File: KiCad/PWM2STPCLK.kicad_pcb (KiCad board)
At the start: 2 copper layers, 21.8 x 16 mm, 8 parts, among them J1 PWM, J2 STPCLK, J3 STPCLK, Q1 2N7002

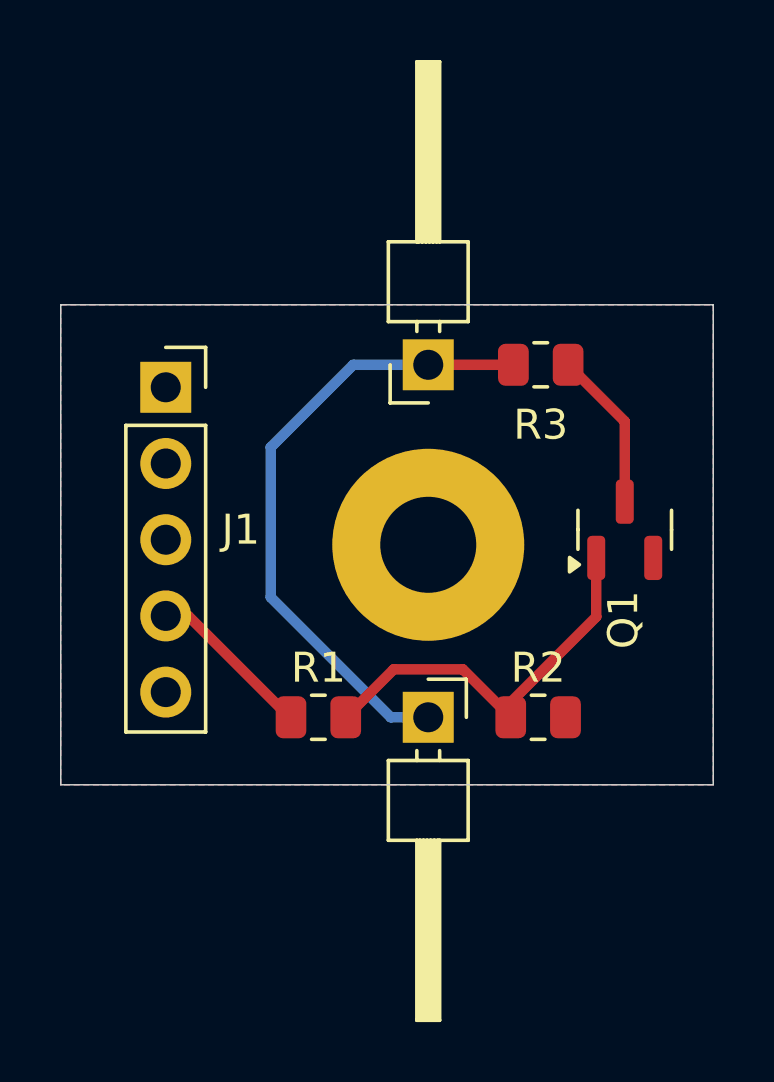
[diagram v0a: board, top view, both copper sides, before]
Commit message: v0.2 - Low resistance ground, cleaner layout
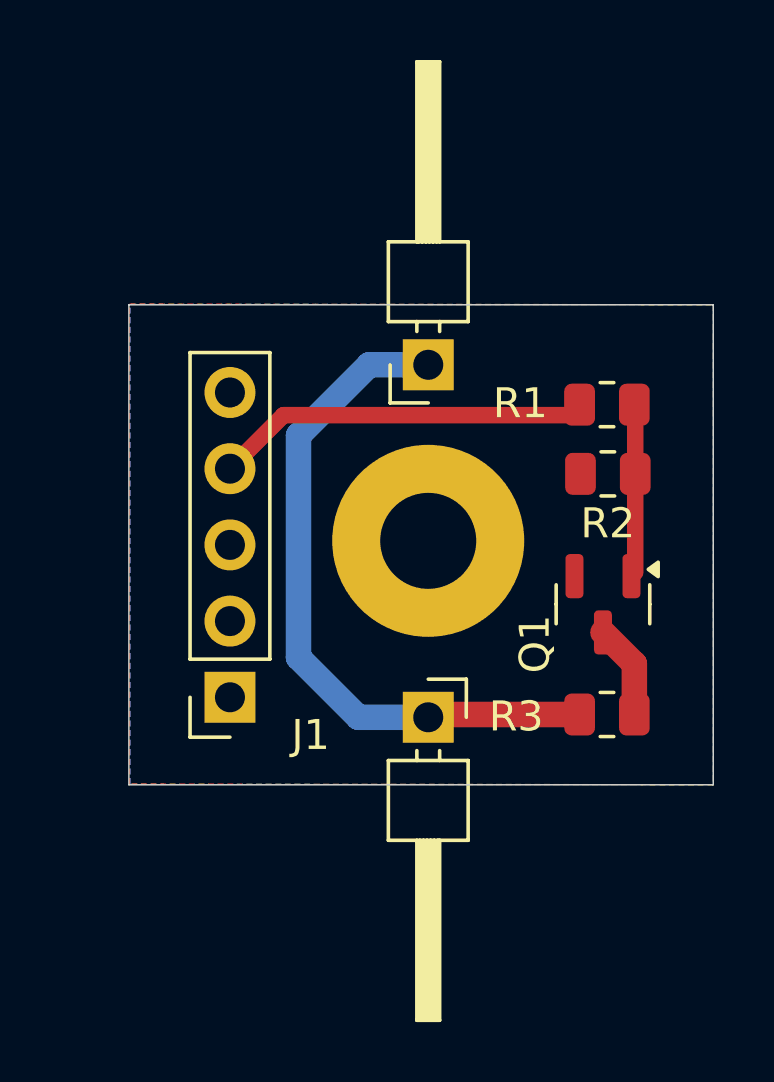
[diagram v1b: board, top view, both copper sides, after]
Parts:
- moved R1 14.2 mm to (157.2, 80.1)
- moved R3 11.9 mm to (157.2, 90.4)
- moved J1 10.6 mm to (144.6, 89.8), turned to 180 degrees
- moved R2 8.44 mm to (157.2, 82.4), turned to 180 degrees
- moved Q1 2.59 mm to (157.1, 86.7), turned to -90 degrees
- moved H1 0.13 mm to (151.2, 84.6)
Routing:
- net Net-(Q1-G): track 13.3 -> 5.78 mm
- net PWM: track 5.58 -> 12.5 mm
- net Net-(Q1-D): track 5.34 -> 3.17 mm
- net STPCLK: track 21.1 -> 22.9 mm
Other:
- board size 21.8 x 16 mm -> 19.5 x 16 mm
- board text added: "PWM2STPCLK v0.2"
